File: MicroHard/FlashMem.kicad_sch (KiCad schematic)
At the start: 5 parts

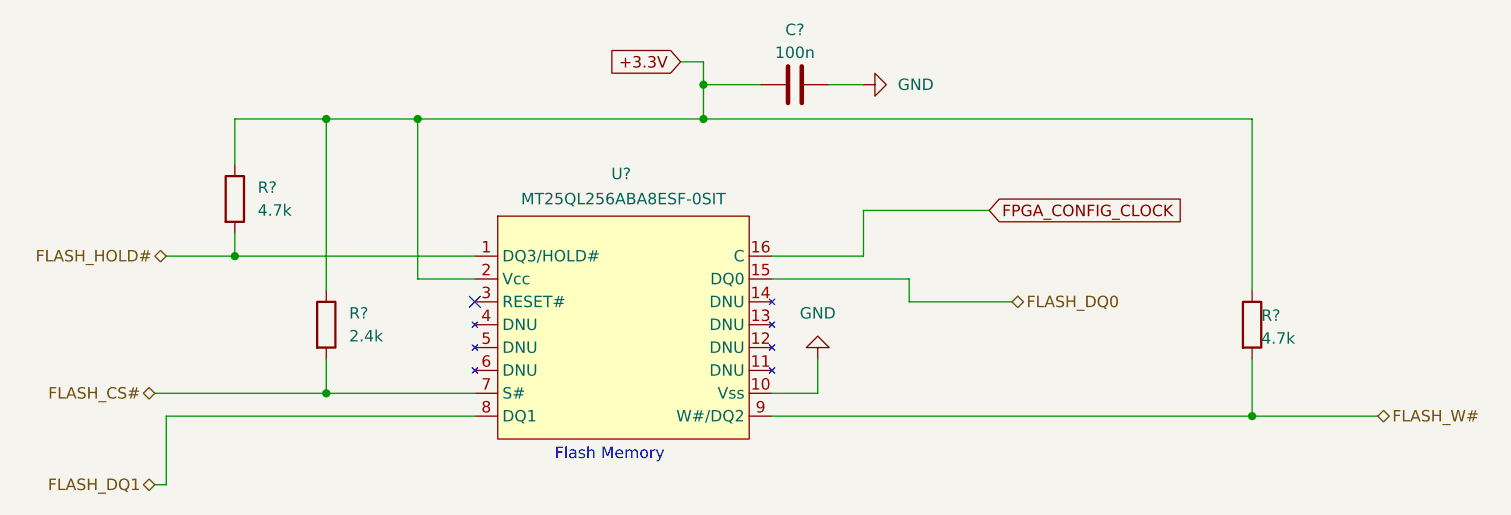
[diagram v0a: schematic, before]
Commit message: Renumber parts
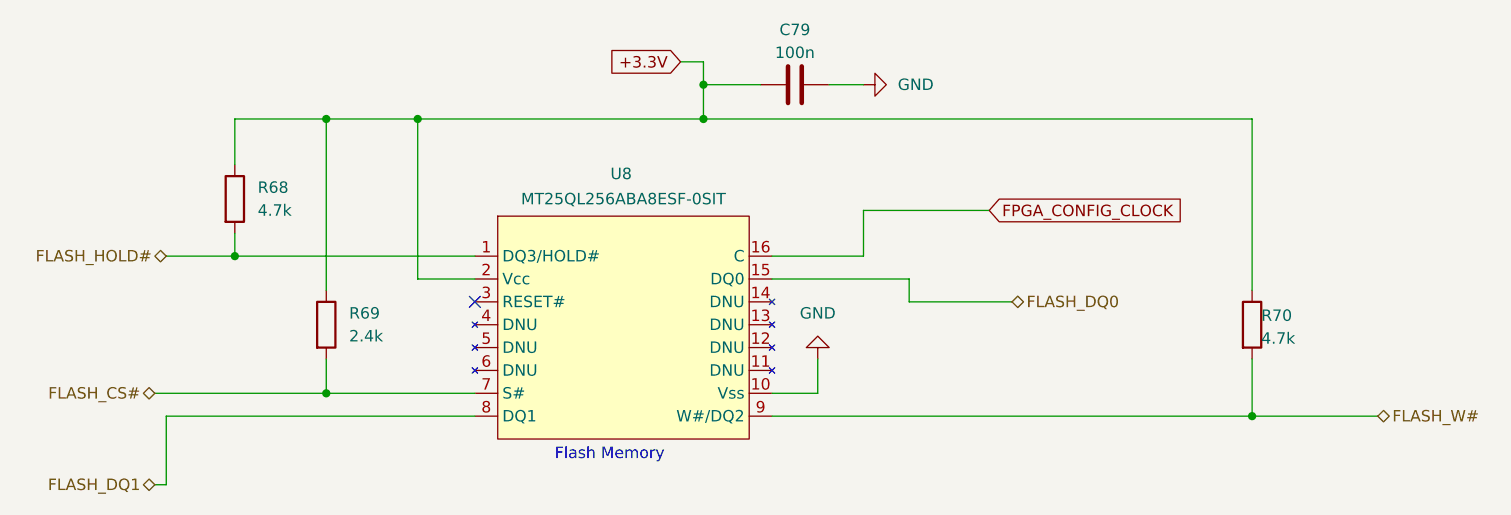
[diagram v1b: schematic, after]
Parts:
- gave numbers to parts that had none: 5
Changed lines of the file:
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@@
 		(dnp no)
 		(fields_autoplaced yes)
-		(property "Reference" "#PWR029"
+		(property "Reference" "#PWR064"
 			(at 142.24 83.82 0)
 			(effects
@@
 			(project "MicroHard"
 				(path "/578bd531-a491-4b15-a479-460d159ffc14/e381883e-e672-4900-88a5-08b94f970a88/1131f32d-45e2-48d4-a5b0-b9e8f8db47f2/85ae7498-e173-4177-8fb1-7abe61a915ce"
-					(reference "#PWR029")
+					(reference "#PWR064")
 					(unit 1)
 				)
@@
 		(on_board yes)
 		(dnp no)
-		(property "Reference" "U?"
+		(property "Reference" "U8"
 			(at 120.396 69.596 0)
 			(effects
@@
 			(project "MicroHard"
 				(path "/578bd531-a491-4b15-a479-460d159ffc14/e381883e-e672-4900-88a5-08b94f970a88/1131f32d-45e2-48d4-a5b0-b9e8f8db47f2/85ae7498-e173-4177-8fb1-7abe61a915ce"
-					(reference "U?")
+					(reference "U8")
 					(unit 1)
 				)
@@
 		(on_board yes)
 		(dnp no)
-		(property "Reference" "C?"
+		(property "Reference" "C79"
 			(at 139.7 53.594 90)
 			(effects
@@
 			(project "MicroHard"
 				(path "/578bd531-a491-4b15-a479-460d159ffc14/e381883e-e672-4900-88a5-08b94f970a88/1131f32d-45e2-48d4-a5b0-b9e8f8db47f2/85ae7498-e173-4177-8fb1-7abe61a915ce"
-					(reference "C?")
+					(reference "C79")
 					(unit 1)
 				)
@@
 		(dnp no)
 		(fields_autoplaced yes)
-		(property "Reference" "R?"
+		(property "Reference" "R69"
 			(at 90.17 85.0899 0)
 			(effects
@@
 			(project "MicroHard"
 				(path "/578bd531-a491-4b15-a479-460d159ffc14/e381883e-e672-4900-88a5-08b94f970a88/1131f32d-45e2-48d4-a5b0-b9e8f8db47f2/85ae7498-e173-4177-8fb1-7abe61a915ce"
-					(reference "R?")
+					(reference "R69")
 					(unit 1)
 				)
@@
 		(dnp no)
 		(fields_autoplaced yes)
-		(property "Reference" "#PWR034"
+		(property "Reference" "#PWR065"
 			(at 153.67 59.69 0)
 			(effects
@@
 			(project "MicroHard"
 				(path "/578bd531-a491-4b15-a479-460d159ffc14/e381883e-e672-4900-88a5-08b94f970a88/1131f32d-45e2-48d4-a5b0-b9e8f8db47f2/85ae7498-e173-4177-8fb1-7abe61a915ce"
-					(reference "#PWR034")
+					(reference "#PWR065")
 					(unit 1)
 				)
@@
 		(on_board yes)
 		(dnp no)
-		(property "Reference" "R?"
+		(property "Reference" "R70"
 			(at 191.516 85.344 0)
 			(effects
@@
 			(project "MicroHard"
 				(path "/578bd531-a491-4b15-a479-460d159ffc14/e381883e-e672-4900-88a5-08b94f970a88/1131f32d-45e2-48d4-a5b0-b9e8f8db47f2/85ae7498-e173-4177-8fb1-7abe61a915ce"
-					(reference "R?")
+					(reference "R70")
 					(unit 1)
 				)
@@
 		(dnp no)
 		(fields_autoplaced yes)
-		(property "Reference" "R?"
+		(property "Reference" "R68"
 			(at 80.01 71.1199 0)
 			(effects
@@
 			(project "MicroHard"
 				(path "/578bd531-a491-4b15-a479-460d159ffc14/e381883e-e672-4900-88a5-08b94f970a88/1131f32d-45e2-48d4-a5b0-b9e8f8db47f2/85ae7498-e173-4177-8fb1-7abe61a915ce"
-					(reference "R?")
-					(unit 1)
-				)
+					(reference "R68")
+					(unit 1)
+				)

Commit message: footprints
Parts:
- C79: footprint (none) -> Capacitor_SMD:C_1206_3216Metric_Pad1.33x1.80mm_HandSolder
- R68, R69, R70: footprint (none) -> Resistor_SMD:R_1206_3216Metric_Pad1.30x1.75mm_HandSolder

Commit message: Initial layout
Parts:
- renumbered C79 to C80, R68 to R69, R69 to R70, R70 to R71
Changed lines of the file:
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@@
 		(dnp no)
 		(fields_autoplaced yes)
-		(property "Reference" "#PWR064"
+		(property "Reference" "#PWR067"
 			(at 142.24 83.82 0)
 			(effects
@@
 			(project "MicroHard"
 				(path "/578bd531-a491-4b15-a479-460d159ffc14/e381883e-e672-4900-88a5-08b94f970a88/1131f32d-45e2-48d4-a5b0-b9e8f8db47f2/85ae7498-e173-4177-8fb1-7abe61a915ce"
-					(reference "#PWR064")
+					(reference "#PWR067")
 					(unit 1)
 				)
@@
 		(on_board yes)
 		(dnp no)
-		(property "Reference" "C79"
+		(property "Reference" "C80"
 			(at 139.7 53.594 90)
 			(effects
@@
 			(project "MicroHard"
 				(path "/578bd531-a491-4b15-a479-460d159ffc14/e381883e-e672-4900-88a5-08b94f970a88/1131f32d-45e2-48d4-a5b0-b9e8f8db47f2/85ae7498-e173-4177-8fb1-7abe61a915ce"
-					(reference "C79")
+					(reference "C80")
 					(unit 1)
 				)
@@
 		(dnp no)
 		(fields_autoplaced yes)
-		(property "Reference" "R69"
+		(property "Reference" "R70"
 			(at 90.17 85.0899 0)
 			(effects
@@
 			(project "MicroHard"
 				(path "/578bd531-a491-4b15-a479-460d159ffc14/e381883e-e672-4900-88a5-08b94f970a88/1131f32d-45e2-48d4-a5b0-b9e8f8db47f2/85ae7498-e173-4177-8fb1-7abe61a915ce"
-					(reference "R69")
+					(reference "R70")
 					(unit 1)
 				)
@@
 		(dnp no)
 		(fields_autoplaced yes)
-		(property "Reference" "#PWR065"
+		(property "Reference" "#PWR066"
 			(at 153.67 59.69 0)
 			(effects
@@
 			(project "MicroHard"
 				(path "/578bd531-a491-4b15-a479-460d159ffc14/e381883e-e672-4900-88a5-08b94f970a88/1131f32d-45e2-48d4-a5b0-b9e8f8db47f2/85ae7498-e173-4177-8fb1-7abe61a915ce"
-					(reference "#PWR065")
+					(reference "#PWR066")
 					(unit 1)
 				)
@@
 		(on_board yes)
 		(dnp no)
-		(property "Reference" "R70"
+		(property "Reference" "R71"
 			(at 191.516 85.344 0)
 			(effects
@@
 			(project "MicroHard"
 				(path "/578bd531-a491-4b15-a479-460d159ffc14/e381883e-e672-4900-88a5-08b94f970a88/1131f32d-45e2-48d4-a5b0-b9e8f8db47f2/85ae7498-e173-4177-8fb1-7abe61a915ce"
-					(reference "R70")
+					(reference "R71")
 					(unit 1)
 				)
@@
 		(dnp no)
 		(fields_autoplaced yes)
-		(property "Reference" "R68"
+		(property "Reference" "R69"
 			(at 80.01 71.1199 0)
 			(effects
@@
 			(project "MicroHard"
 				(path "/578bd531-a491-4b15-a479-460d159ffc14/e381883e-e672-4900-88a5-08b94f970a88/1131f32d-45e2-48d4-a5b0-b9e8f8db47f2/85ae7498-e173-4177-8fb1-7abe61a915ce"
-					(reference "R68")
+					(reference "R69")
 					(unit 1)
 				)

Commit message: Fix schematics for delivery
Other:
- company: (none) -> MicroHard
- title: (none) -> FPGA Flash Memory
